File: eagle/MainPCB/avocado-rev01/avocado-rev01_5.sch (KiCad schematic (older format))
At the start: 33 parts, among them U2 AP65111A, U3 AP65111A, U4 AP65111A

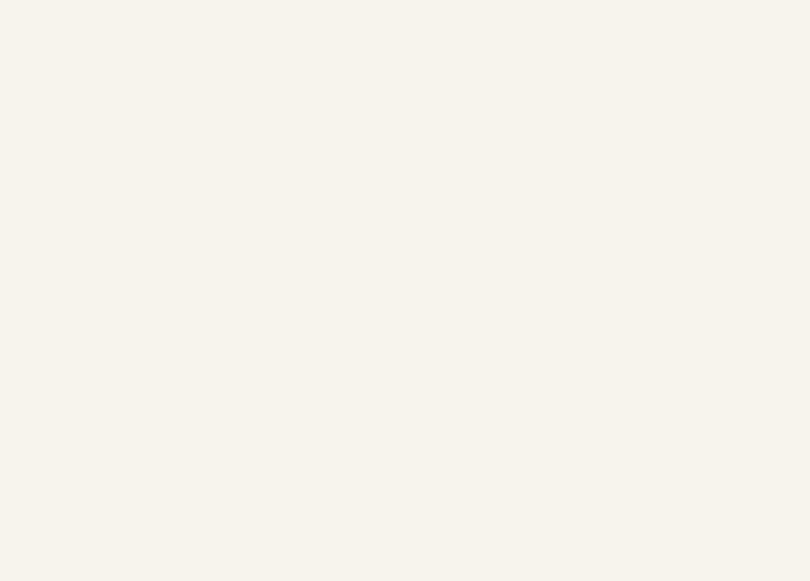
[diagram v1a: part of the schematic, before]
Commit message: added 3V rail
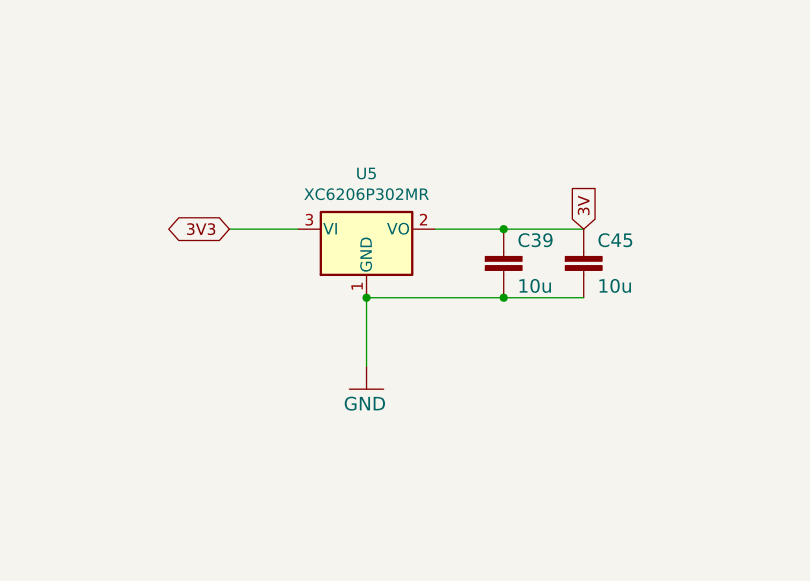
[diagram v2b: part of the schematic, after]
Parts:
- added C39, C45: 10u, avocado-rev01:C0603, symbol avocado-rev01-eagle-import:C0603
- added U5: XC6206P302MR, Package_TO_SOT_SMD:SOT-23, symbol Regulator_Linear:MCP1703A-3002_SOT23
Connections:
- net 3V3: now also U5.3 (VI)
- new net: C39.2, C45.2, U5.1 (GND)
- new net 3V: C39.1, C45.1, U5.2 (VO)
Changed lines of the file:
@@
 $Descr User 12095 8633
 encoding utf-8
-Sheet 1 6
+Sheet 6 6
 Title ""
 Date ""
@@
 	0    -1   -1   0
 $EndComp
+$Comp
+L Regulator_Linear:MCP1703A-3002_SOT23 U5
+U 1 1 5C871AAE
+P 8100 2600
+F 0 "U5" H 8100 2842 50  0000 C CNN
+F 1 "XC6206P302MR" H 8100 2751 50  0000 C CNN
+F 2 "Package_TO_SOT_SMD:SOT-23" H 8100 2800 50  0001 C CNN
+F 3 "http://ww1.microchip.com/downloads/en/DeviceDoc/20005122B.pdf" H 8100 2550 50  0001 C CNN
+	1    8100 2600
+	1    0    0    -1
+$EndComp
+Text GLabel 7500 2600 0    50   BiDi ~ 0
+3V3
+Wire Wire Line
+	7800 2600 7500 2600
+$Comp
+L avocado-rev01-eagle-import:C0603 C?
+U 1 0 5C875E54
+P 8700 2700
+AR Path="/5C875E54" Ref="C?"  Part="1"
+AR Path="/5C85FF4A/5C875E54" Ref="C39"  Part="1"
+F 0 "C39" H 8760 2715 59  0000 L BNN
+F 1 "10u" H 8760 2515 59  0000 L BNN
+F 2 "avocado-rev01:C0603" H 8700 2700 50  0001 C CNN
+F 3 "" H 8700 2700 50  0001 C CNN
+	1    8700 2700
+	1    0    0    -1
+$EndComp
+$Comp
+L avocado-rev01-eagle-import:C0603 C?
+U 1 0 5C876EE9
+P 9050 2700
+AR Path="/5C876EE9" Ref="C?"  Part="1"
+AR Path="/5C85FF4A/5C876EE9" Ref="C45"  Part="1"
+F 0 "C45" H 9110 2715 59  0000 L BNN
+F 1 "10u" H 9110 2515 59  0000 L BNN
+F 2 "avocado-rev01:C0603" H 9050 2700 50  0001 C CNN
+F 3 "" H 9050 2700 50  0001 C CNN
+	1    9050 2700
+	1    0    0    -1
+$EndComp
+Wire Wire Line
+	9050 2600 8700 2600
+Connection ~ 8700 2600
+Wire Wire Line
+	8700 2600 8400 2600
+Wire Wire Line
+	9050 2900 8700 2900
+Wire Wire Line
+	8700 2900 8100 2900
+Connection ~ 8700 2900
+Wire Wire Line
+	8100 2900 8100 3200
+Connection ~ 8100 2900
+$Comp
+L avocado-rev01-eagle-import:GND #GND?
+U 1 0 5C888656
+P 8100 3300
+AR Path="/5C888656" Ref="#GND?"  Part="1"
+AR Path="/5C85FF4A/5C888656" Ref="#GND0106"  Part="1"
+F 0 "#GND0106" H 8100 3300 50  0001 C CNN
+F 1 "GND" H 8000 3200 59  0000 L BNN
+F 2 "" H 8100 3300 50  0001 C CNN
+F 3 "" H 8100 3300 50  0001 C CNN
+	1    8100 3300
+	1    0    0    -1
+$EndComp
+Text GLabel 9050 2600 1    50   Input ~ 0
+3V
 $EndSCHEMATC
